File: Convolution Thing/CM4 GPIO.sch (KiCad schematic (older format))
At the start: 1 part

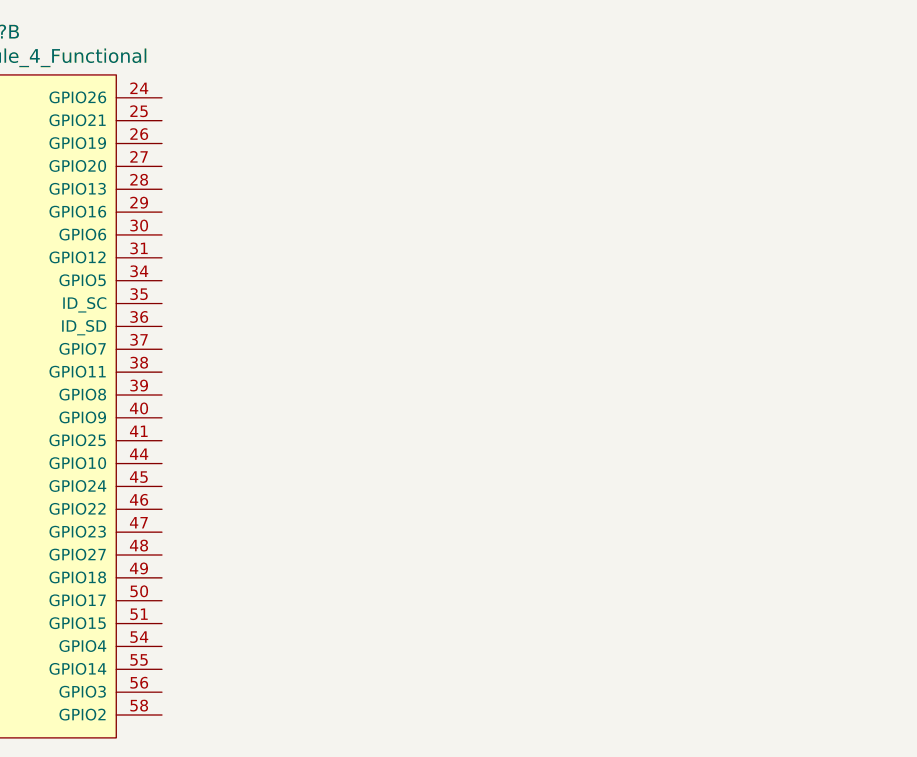
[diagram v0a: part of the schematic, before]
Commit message: Audio I/O, CV input, GPIO work & misc changes
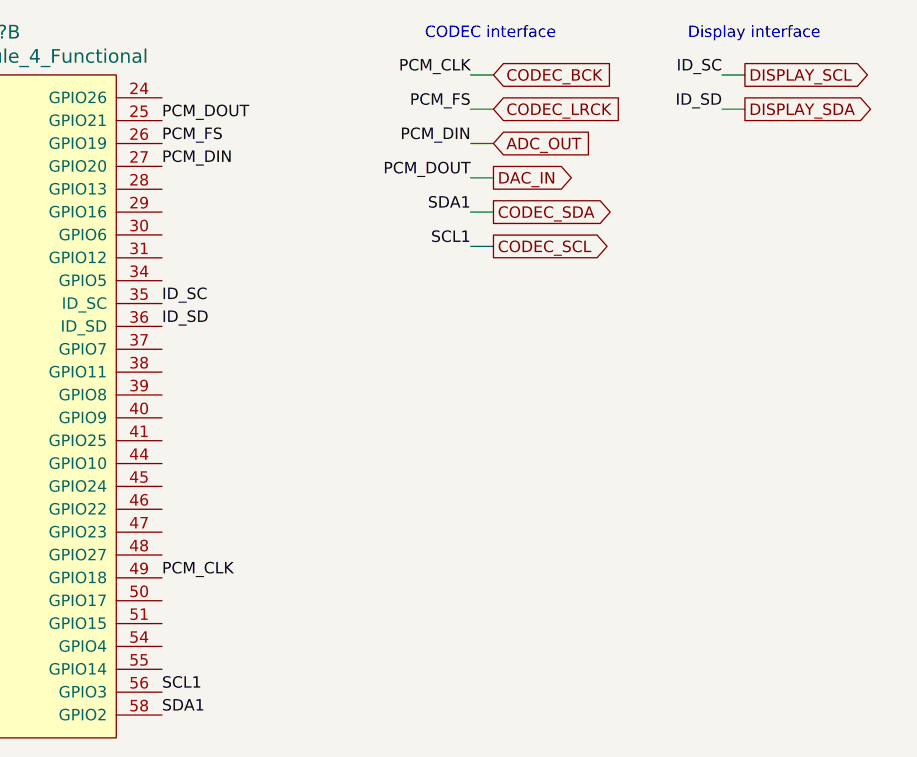
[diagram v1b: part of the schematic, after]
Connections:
- net DAC_IN: now reaches U?.25 (GPIO21)
- net CODEC_LRCK: now reaches U?.26 (GPIO19)
- net ADC_OUT: now reaches U?.27 (GPIO20)
- net DISPLAY_SCL: now reaches U?.35 (ID_SC)
- net DISPLAY_SDA: now reaches U?.36 (ID_SD)
- net CODEC_BCK: now reaches U?.49 (GPIO18)
- net CODEC_SCL: now reaches U?.56 (GPIO3)
- net CODEC_SDA: now reaches U?.58 (GPIO2)
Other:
- note added: "CODEC interface"
- note added: "Display interface"
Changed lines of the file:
@@
 $Descr A4 11693 8268
 encoding utf-8
-Sheet 5 7
+Sheet 5 9
 Title ""
 Date ""
@@
 	1    0    0    -1
 $EndComp
+Text Label 2050 3200 0    50   ~ 0
+PCM_CLK
+Text Label 2050 1300 0    50   ~ 0
+PCM_FS
+Text Label 2050 1400 0    50   ~ 0
+PCM_DIN
+Text Label 2050 1200 0    50   ~ 0
+PCM_DOUT
+Text GLabel 3500 1450 2    50   Output ~ 0
+DAC_IN
+Text GLabel 3500 1300 2    50   Input ~ 0
+ADC_OUT
+Text GLabel 3500 1000 2    50   Input ~ 0
+CODEC_BCK
+Text GLabel 3500 1150 2    50   Input ~ 0
+CODEC_LRCK
+Text Label 3400 1450 2    50   ~ 0
+PCM_DOUT
+Text Label 3400 1150 2    50   ~ 0
+PCM_FS
+Text Label 3400 1300 2    50   ~ 0
+PCM_DIN
+Text Label 3400 1000 2    50   ~ 0
+PCM_CLK
+Wire Wire Line
+	3400 1000 3500 1000
+Wire Wire Line
+	3500 1150 3400 1150
+Wire Wire Line
+	3400 1300 3500 1300
+Wire Wire Line
+	3500 1450 3400 1450
+Text Notes 3200 850  0    50   ~ 0
+CODEC interface
+Text Label 3400 1750 2    50   ~ 0
+SCL1
+Text Label 3400 1600 2    50   ~ 0
+SDA1
+Text GLabel 3500 1750 2    50   Output ~ 0
+CODEC_SCL
+Text GLabel 3500 1600 2    50   Output ~ 0
+CODEC_SDA
+Wire Wire Line
+	3500 1600 3400 1600
+Wire Wire Line
+	3400 1750 3500 1750
+Text Label 2050 3700 0    50   ~ 0
+SCL1
+Text Label 2050 3800 0    50   ~ 0
+SDA1
+Text Label 2050 2000 0    50   ~ 0
+ID_SC
+Text Label 2050 2100 0    50   ~ 0
+ID_SD
+Text Notes 4350 850  0    50   ~ 0
+Display interface
+Text Label 4500 1000 2    50   ~ 0
+ID_SC
+Text Label 4500 1150 2    50   ~ 0
+ID_SD
+Text GLabel 4600 1000 2    50   Output ~ 0
+DISPLAY_SCL
+Text GLabel 4600 1150 2    50   Output ~ 0
+DISPLAY_SDA
+Wire Wire Line
+	4600 1150 4500 1150
+Wire Wire Line
+	4500 1000 4600 1000
 $EndSCHEMATC

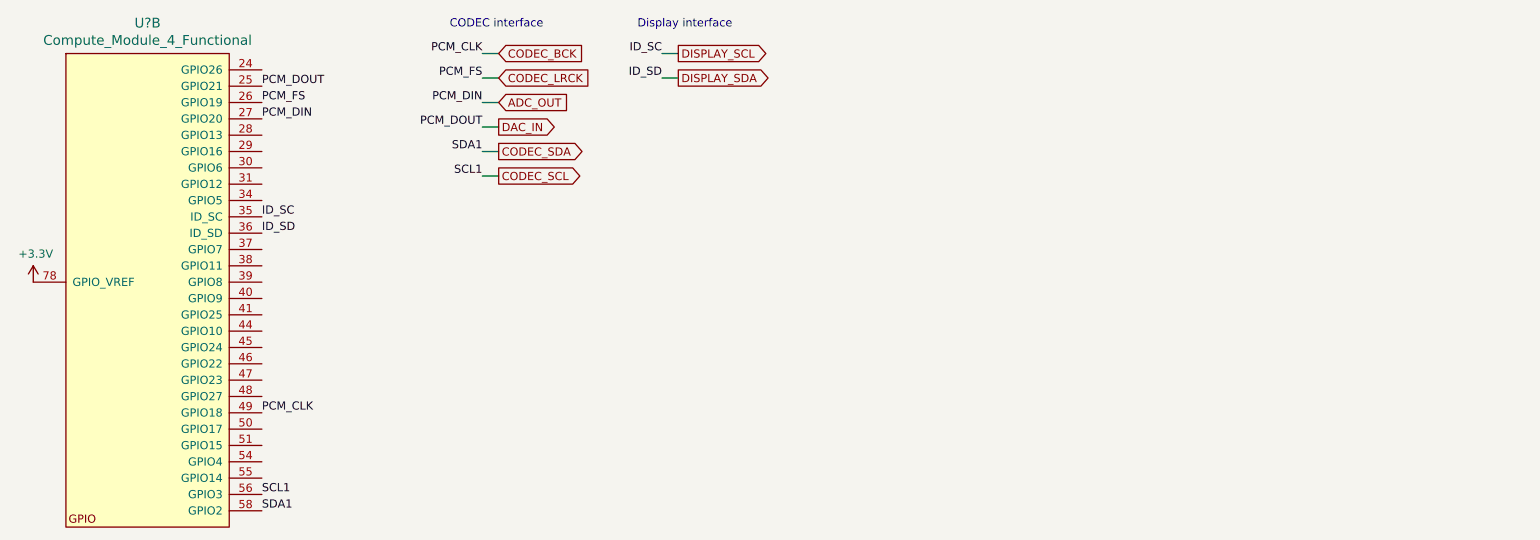
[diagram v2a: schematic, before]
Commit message: Added gate inputs and CM4 / display sockets, made CV inputs 100k, lots of smaller changes. First iteration of schematic now done.
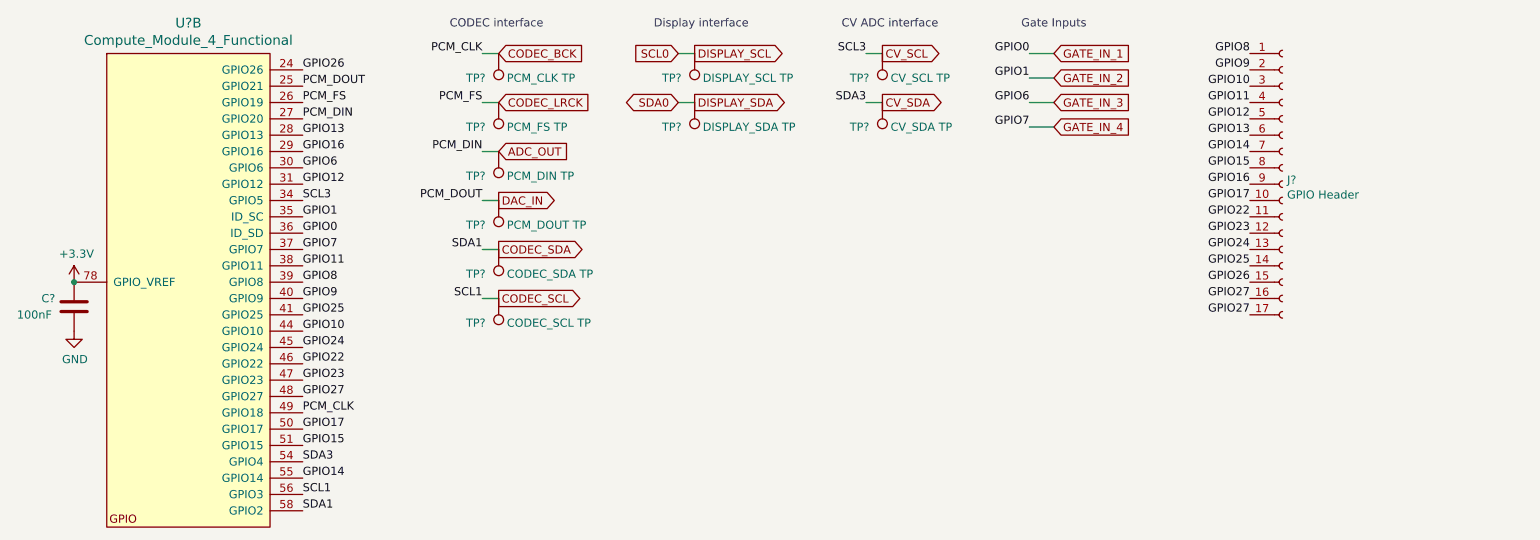
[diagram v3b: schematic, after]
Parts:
- added C?: 100nF, symbol Device:C
- added J?: GPIO Header, symbol Connector:Conn_01x17_Female
- added TP?: PCM_CLK TP, symbol Connector:TestPoint
- added TP?: PCM_FS TP, symbol Connector:TestPoint
- added TP?: PCM_DIN TP, symbol Connector:TestPoint
- added TP?: PCM_DOUT TP, symbol Connector:TestPoint
- added TP?: CODEC_SDA TP, symbol Connector:TestPoint
- added TP?: CODEC_SCL TP, symbol Connector:TestPoint
- added TP?: DISPLAY_SCL TP, symbol Connector:TestPoint
- added TP?: DISPLAY_SDA TP, symbol Connector:TestPoint
- added TP?: CV_SCL TP, symbol Connector:TestPoint
- added TP?: CV_SDA TP, symbol Connector:TestPoint
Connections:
- net +3V3: now also C?.1
- net ADC_OUT: now also TP?.1
- net CODEC_BCK: now also TP?.1
- net CODEC_LRCK: now also TP?.1
- net CODEC_SCL: now also TP?.1
- net CODEC_SDA: now also TP?.1
- net DAC_IN: now also TP?.1
- net DISPLAY_SCL: now also TP?.1; no longer U?.35 (ID_SC)
- net DISPLAY_SDA: now also TP?.1; no longer U?.36 (ID_SD)
- net GPIO26: now reaches U?.24 (GPIO26)
- net GPIO26: now also J?.15 (Pin_15)
- net GPIO13: now reaches U?.28 (GPIO13)
- net GPIO13: now also J?.6 (Pin_6)
- net GPIO16: now reaches U?.29 (GPIO16)
- net GPIO16: now also J?.9 (Pin_9)
- net GATE_IN_3: now reaches U?.30 (GPIO6)
- net GPIO12: now reaches U?.31 (GPIO12)
- net GPIO12: now also J?.5 (Pin_5)
- net CV_SCL: now reaches U?.34 (GPIO5)
- net CV_SCL: now also TP?.1
- net GATE_IN_4: now reaches U?.37 (GPIO7)
- net GPIO11: now reaches U?.38 (GPIO11)
- net GPIO11: now also J?.4 (Pin_4)
- net GPIO8: now reaches U?.39 (GPIO8)
- net GPIO8: now also J?.1 (Pin_1)
- net GPIO9: now reaches U?.40 (GPIO9)
- net GPIO9: now also J?.2 (Pin_2)
- net GPIO25: now reaches U?.41 (GPIO25)
- net GPIO25: now also J?.14 (Pin_14)
- net GPIO10: now reaches U?.44 (GPIO10)
- net GPIO10: now also J?.3 (Pin_3)
- net GPIO24: now reaches U?.45 (GPIO24)
- net GPIO24: now also J?.13 (Pin_13)
- net GPIO22: now reaches U?.46 (GPIO22)
- net GPIO22: now also J?.11 (Pin_11)
- net GPIO23: now reaches U?.47 (GPIO23)
- net GPIO23: now also J?.12 (Pin_12)
- net GPIO27: now reaches U?.48 (GPIO27)
- net GPIO27: now also J?.16 (Pin_16), J?.17 (Pin_17)
- net GPIO17: now reaches U?.50 (GPIO17)
- net GPIO17: now also J?.10 (Pin_10)
- net GPIO15: now reaches U?.51 (GPIO15)
- net GPIO15: now also J?.8 (Pin_8)
- net CV_SDA: now reaches U?.54 (GPIO4)
- net CV_SDA: now also TP?.1
- net GPIO14: now reaches U?.55 (GPIO14)
- net GPIO14: now also J?.7 (Pin_7)
- new net GATE_IN_1: U?.36 (ID_SD)
- new net GATE_IN_2: U?.35 (ID_SC)
- new net GND: C?.2
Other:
- note added: "CV ADC interface"
- note added: "Gate Inputs"
- moved on the sheet: U?B

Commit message: Fix some issues, add component references
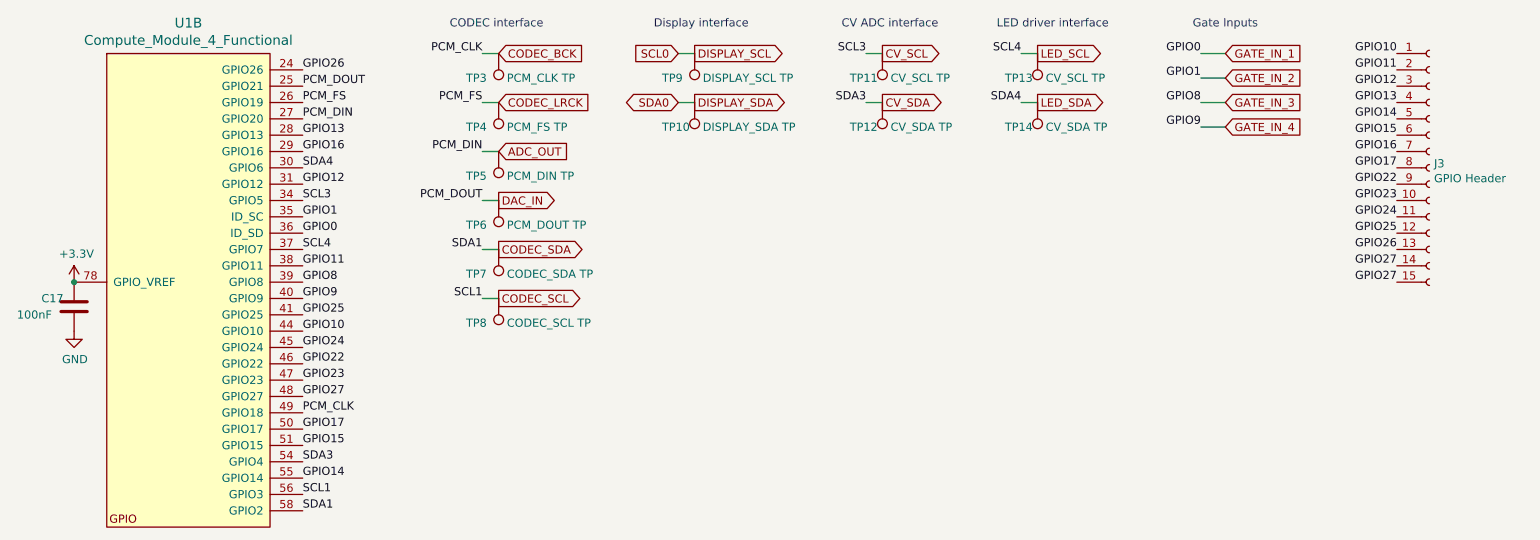
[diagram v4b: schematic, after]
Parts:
- removed J?: GPIO Header, symbol Connector:Conn_01x17_Female
- added J3: GPIO Header, symbol Connector:Conn_01x15_Female
- added TP13: CV_SCL TP, symbol Connector:TestPoint
- added TP14: CV_SDA TP, symbol Connector:TestPoint
- gave numbers to parts that had none: 12
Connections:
- net GPIO8 is gone; now on net GATE_IN_3: U1.39 (GPIO8)
- net GPIO9 is gone; now on net GATE_IN_4: U1.40 (GPIO9)
- net GATE_IN_3: no longer U1.30 (GPIO6)
- net GATE_IN_4: no longer U1.37 (GPIO7)
- net GPIO10: now also J3.1 (Pin_1)
- net GPIO11: now also J3.2 (Pin_2)
- net GPIO12: now also J3.3 (Pin_3)
- net GPIO13: now also J3.4 (Pin_4)
- net GPIO14: now also J3.5 (Pin_5)
- net GPIO15: now also J3.6 (Pin_6)
- net GPIO16: now also J3.7 (Pin_7)
- net GPIO17: now also J3.8 (Pin_8)
- net GPIO22: now also J3.9 (Pin_9)
- net GPIO23: now also J3.10 (Pin_10)
- net GPIO24: now also J3.11 (Pin_11)
- net GPIO25: now also J3.12 (Pin_12)
- net GPIO26: now also J3.13 (Pin_13)
- net GPIO27: now also J3.14 (Pin_14), J3.15 (Pin_15)
- new net LED_SCL: TP13.1, U1.37 (GPIO7)
- new net LED_SDA: TP14.1, U1.30 (GPIO6)
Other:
- note added: "LED driver interface"
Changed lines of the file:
@@
 $EndDescr
 $Comp
-L CM4:Compute_Module_4_Functional U?
+L CM4:Compute_Module_4_Functional U1
 U 2 1 61088AAE
 P 900 1100
-F 0 "U?" H 1600 1387 60  0000 C CNN
+F 0 "U1" H 1600 1387 60  0000 C CNN
 F 1 "Compute_Module_4_Functional" H 1600 1281 60  0000 C CNN
 F 2 "" H 1100 1150 60  0001 L CNN
@@
 $EndComp
 $Comp
-L power:+3.3V #PWR?
+L power:+3.3V #PWR039
 U 1 1 6108F224
 P 900 2400
-F 0 "#PWR?" H 900 2250 50  0001 C CNN
+F 0 "#PWR039" H 900 2250 50  0001 C CNN
 F 1 "+3.3V" H 915 2573 50  0000 C CNN
 F 2 "" H 900 2400 50  0001 C CNN
@@
 GPIO11
 Text Label 2300 2200 0    50   ~ 0
-GPIO7
+SCL4
 Text Label 2300 1800 0    50   ~ 0
 GPIO12
 Text Label 2300 1700 0    50   ~ 0
-GPIO6
+SDA4
 Text Label 2300 1600 0    50   ~ 0
 GPIO16
 Text Label 2300 1500 0    50   ~ 0
 GPIO13
-Text Notes 6700 850  0    50   ~ 0
+Text Notes 7750 850  0    50   ~ 0
 Gate Inputs
-Text Label 6750 1000 2    50   ~ 0
+Text Label 7800 1000 2    50   ~ 0
 GPIO0
-Text GLabel 6900 1000 2    50   Input ~ 0
+Text GLabel 7950 1000 2    50   Input ~ 0
 GATE_IN_1
 Wire Wire Line
-	6750 1000 6900 1000
+	7800 1000 7950 1000
 Text Label 2300 1100 0    50   ~ 0
 GPIO26
-Text Label 8100 1000 2    50   ~ 0
-GPIO8
-Text Label 8100 1100 2    50   ~ 0
-GPIO9
-Text Label 8100 1200 2    50   ~ 0
+Text Label 9000 1000 2    50   ~ 0
 GPIO10
-Text Label 8100 1300 2    50   ~ 0
+Text Label 9000 1100 2    50   ~ 0
 GPIO11
-Text Label 8100 1400 2    50   ~ 0
+Text Label 9000 1200 2    50   ~ 0
 GPIO12
-Text Label 8100 1500 2    50   ~ 0
+Text Label 9000 1300 2    50   ~ 0
 GPIO13
-Text Label 8100 1600 2    50   ~ 0
+Text Label 9000 1400 2    50   ~ 0
 GPIO14
-Text Label 8100 1700 2    50   ~ 0
+Text Label 9000 1500 2    50   ~ 0
 GPIO15
-Text Label 8100 1800 2    50   ~ 0
+Text Label 9000 1600 2    50   ~ 0
 GPIO16
-Text Label 8100 1900 2    50   ~ 0
+Text Label 9000 1700 2    50   ~ 0
 GPIO17
-Text Label 8100 2000 2    50   ~ 0
+Text Label 9000 1800 2    50   ~ 0
 GPIO22
-Text Label 8100 2100 2    50   ~ 0
+Text Label 9000 1900 2    50   ~ 0
 GPIO23
-Text Label 8100 2200 2    50   ~ 0
+Text Label 9000 2000 2    50   ~ 0
 GPIO24
-Text Label 8100 2300 2    50   ~ 0
+Text Label 9000 2100 2    50   ~ 0
 GPIO25
-Text Label 8100 2400 2    50   ~ 0
+Text Label 9000 2200 2    50   ~ 0
 GPIO26
-Text Label 8100 2500 2    50   ~ 0
+Text Label 9000 2300 2    50   ~ 0
 GPIO27
-Text Label 8100 2600 2    50   ~ 0
+Text Label 9000 2400 2    50   ~ 0
 GPIO27
 $Comp
-L Connector:TestPoint TP?
+L Connector:TestPoint TP3
 U 1 1 6117ED3E
 P 3500 1000
-F 0 "TP?" H 3700 1150 50  0000 R CNN
+F 0 "TP3" H 3700 1150 50  0000 R CNN
 F 1 "PCM_CLK TP" H 3450 1150 50  0000 R CNN
 F 2 "" H 3700 1000 50  0001 C CNN
@@
 $EndComp
 $Comp
-L Connector:TestPoint TP?
+L Connector:TestPoint TP4
 U 1 1 61180804
 P 3500 1300
-F 0 "TP?" H 3700 1450 50  0000 R CNN
+F 0 "TP4" H 3700 1450 50  0000 R CNN
 F 1 "PCM_FS TP" H 3450 1450 50  0000 R CNN
 F 2 "" H 3700 1300 50  0001 C CNN
@@
 $EndComp
 $Comp
-L Connector:TestPoint TP?
+L Connector:TestPoint TP5
 U 1 1 61180A43
 P 3500 1600
-F 0 "TP?" H 3700 1750 50  0000 R CNN
+F 0 "TP5" H 3700 1750 50  0000 R CNN
 F 1 "PCM_DIN TP" H 3450 1750 50  0000 R CNN
 F 2 "" H 3700 1600 50  0001 C CNN
@@
 $EndComp
 $Comp
-L Connector:TestPoint TP?
+L Connector:TestPoint TP6
 U 1 1 61180F4D
 P 3500 1900
-F 0 "TP?" H 3700 2050 50  0000 R CNN
+F 0 "TP6" H 3700 2050 50  0000 R CNN
 F 1 "PCM_DOUT TP" H 3450 2050 50  0000 R CNN
 F 2 "" H 3700 1900 50  0001 C CNN
@@
 $EndComp
 $Comp
-L Connector:TestPoint TP?
+L Connector:TestPoint TP7
 U 1 1 61181263
 P 3500 2200
-F 0 "TP?" H 3700 2350 50  0000 R CNN
+F 0 "TP7" H 3700 2350 50  0000 R CNN
 F 1 "CODEC_SDA TP" H 3450 2350 50  0000 R CNN
 F 2 "" H 3700 2200 50  0001 C CNN
@@
 $EndComp
 $Comp
-L Connector:TestPoint TP?
+L Connector:TestPoint TP8
 U 1 1 611813BD
 P 3500 2500
-F 0 "TP?" H 3700 2650 50  0000 R CNN
+F 0 "TP8" H 3700 2650 50  0000 R CNN
 F 1 "CODEC_SCL TP" H 3450 2650 50  0000 R CNN
 F 2 "" H 3700 2500 50  0001 C CNN
@@
 $EndComp
 $Comp
-L Connector:TestPoint TP?
+L Connector:TestPoint TP9
 U 1 1 61182752
 P 4700 1000
-F 0 "TP?" H 4900 1150 50  0000 R CNN
+F 0 "TP9" H 4900 1150 50  0000 R CNN
 F 1 "DISPLAY_SCL TP" H 4650 1150 50  0000 R CNN
 F 2 "" H 4900 1000 50  0001 C CNN
@@
 $EndComp
 $Comp
-L Connector:TestPoint TP?
+L Connector:TestPoint TP10
 U 1 1 6118398B
 P 4700 1300
-F 0 "TP?" H 4900 1450 50  0000 R CNN
+F 0 "TP10" H 4900 1450 50  0000 R CNN
 F 1 "DISPLAY_SDA TP" H 4650 1450 50  0000 R CNN
 F 2 "" H 4900 1300 50  0001 C CNN
@@
 $EndComp
 Wire Wire Line
-	6900 1150 6750 1150
-Wire Wire Line
-	6750 1300 6900 1300
-Wire Wire Line
-	6900 1450 6750 1450
-Text GLabel 6900 1450 2    50   Input ~ 0
+	7950 1150 7800 1150
+Wire Wire Line
+	7800 1300 7950 1300
+Wire Wire Line
+	7950 1450 7800 1450
+Text GLabel 7950 1450 2    50   Input ~ 0
 GATE_IN_4
-Text GLabel 6900 1300 2    50   Input ~ 0
+Text GLabel 7950 1300 2    50   Input ~ 0
 GATE_IN_3
-Text GLabel 6900 1150 2    50   Input ~ 0
+Text GLabel 7950 1150 2    50   Input ~ 0
 GATE_IN_2
-Text Label 6750 1450 2    50   ~ 0
-GPIO7
-Text Label 6750 1300 2    50   ~ 0
-GPIO6
-Text Label 6750 1150 2    50   ~ 0
+Text Label 7800 1450 2    50   ~ 0
+GPIO9
+Text Label 7800 1300 2    50   ~ 0
+GPIO8
+Text Label 7800 1150 2    50   ~ 0
 GPIO1
 Text Notes 5600 850  0    50   ~ 0
@@
 	5750 1000 5850 1000
 $Comp
-L Connector:TestPoint TP?
+L Connector:TestPoint TP11
 U 1 1 6118C1D0
 P 5850 1000
-F 0 "TP?" H 6050 1150 50  0000 R CNN
+F 0 "TP11" H 6050 1150 50  0000 R CNN
 F 1 "CV_SCL TP" H 5800 1150 50  0000 R CNN
 F 2 "" H 6050 1000 50  0001 C CNN
@@
 $EndComp
 $Comp
-L Connector:TestPoint TP?
+L Connector:TestPoint TP12
 U 1 1 6118C1D6
 P 5850 1300
-F 0 "TP?" H 6050 1450 50  0000 R CNN
+F 0 "TP12" H 6050 1450 50  0000 R CNN
 F 1 "CV_SDA TP" H 5800 1450 50  0000 R CNN
 F 2 "" H 6050 1300 50  0001 C CNN
@@
 SCL3
 $Comp
-L Connector:Conn_01x17_Female J?
-U 1 1 611A5A43
-P 8300 1800
-F 0 "J?" H 8328 1826 50  0000 L CNN
-F 1 "GPIO Header" H 8328 1735 50  0000 L CNN
-F 2 "" H 8300 1800 50  0001 C CNN
-F 3 "~" H 8300 1800 50  0001 C CNN
-	1    8300 1800
-	1    0    0    -1
-$EndComp
-$Comp
-L Device:C C?
+L Device:C C17
 U 1 1 612C059D
 P 900 2550
-F 0 "C?" H 1100 2600 50  0000 R CNN
+F 0 "C17" H 1100 2600 50  0000 R CNN
 F 1 "100nF" H 1250 2500 50  0000 R CNN
 F 2 "" H 938 2400 50  0001 C CNN
@@
 Connection ~ 900  2400
 $Comp
-L power:GND #PWR?
+L power:GND #PWR040
 U 1 1 612C15EE
 P 900 2700
-F 0 "#PWR?" H 900 2450 50  0001 C CNN
+F 0 "#PWR040" H 900 2450 50  0001 C CNN
 F 1 "GND" H 905 2527 50  0000 C CNN
 F 2 "" H 900 2700 50  0001 C CNN
@@
 	1    0    0    -1
 $EndComp
+Text Notes 6550 850  0    50   ~ 0
+LED driver interface
+Text Label 6700 1000 2    50   ~ 0
+SCL4
+Text Label 6700 1300 2    50   ~ 0
+SDA4
+Text GLabel 6800 1000 2    50   Output ~ 0
+LED_SCL
+Text GLabel 6800 1300 2    50   Output ~ 0
+LED_SDA
+Wire Wire Line
+	6800 1300 6700 1300
+Wire Wire Line
+	6700 1000 6800 1000
+$Comp
+L Connector:TestPoint TP13
+U 1 1 610FBC13
+P 6800 1000
+F 0 "TP13" H 7000 1150 50  0000 R CNN
+F 1 "CV_SCL TP" H 6750 1150 50  0000 R CNN
+F 2 "" H 7000 1000 50  0001 C CNN
+F 3 "~" H 7000 1000 50  0001 C CNN
+	1    6800 1000
+	-1   0    0    1
+$EndComp
+$Comp
+L Connector:TestPoint TP14
+U 1 1 610FBC19
+P 6800 1300
+F 0 "TP14" H 7000 1450 50  0000 R CNN
+F 1 "CV_SDA TP" H 6750 1450 50  0000 R CNN
+F 2 "" H 7000 1300 50  0001 C CNN
+F 3 "~" H 7000 1300 50  0001 C CNN
+	1    6800 1300
+	-1   0    0    1
+$EndComp
+$Comp
+L Connector:Conn_01x15_Female J3
+U 1 1 61101298
+P 9200 1700
+F 0 "J3" H 9228 1726 50  0000 L CNN
+F 1 "GPIO Header" H 9228 1635 50  0000 L CNN
+F 2 "" H 9200 1700 50  0001 C CNN
+F 3 "~" H 9200 1700 50  0001 C CNN
+	1    9200 1700
+	1    0    0    -1
+$EndComp
